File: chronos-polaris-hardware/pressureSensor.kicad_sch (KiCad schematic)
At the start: 3 parts, among them U9 BMP280

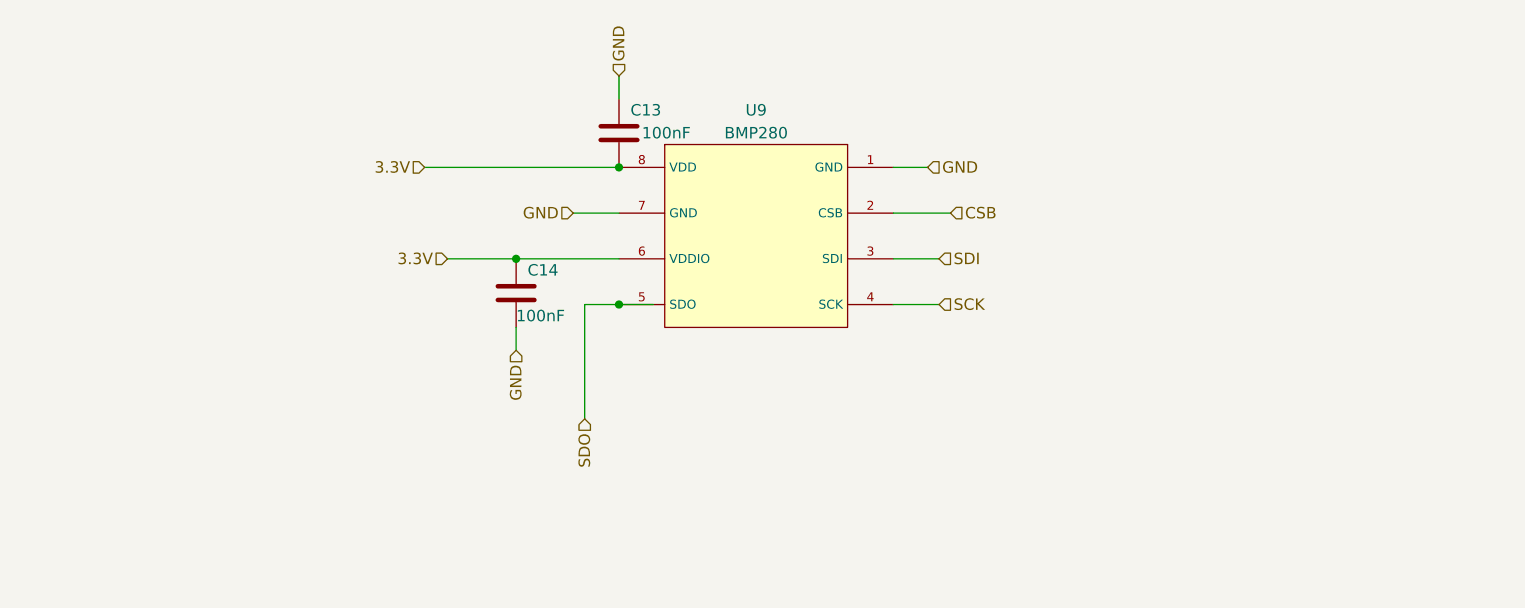
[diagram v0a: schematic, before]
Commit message: Schematic Changes as per DR1 Suggestions
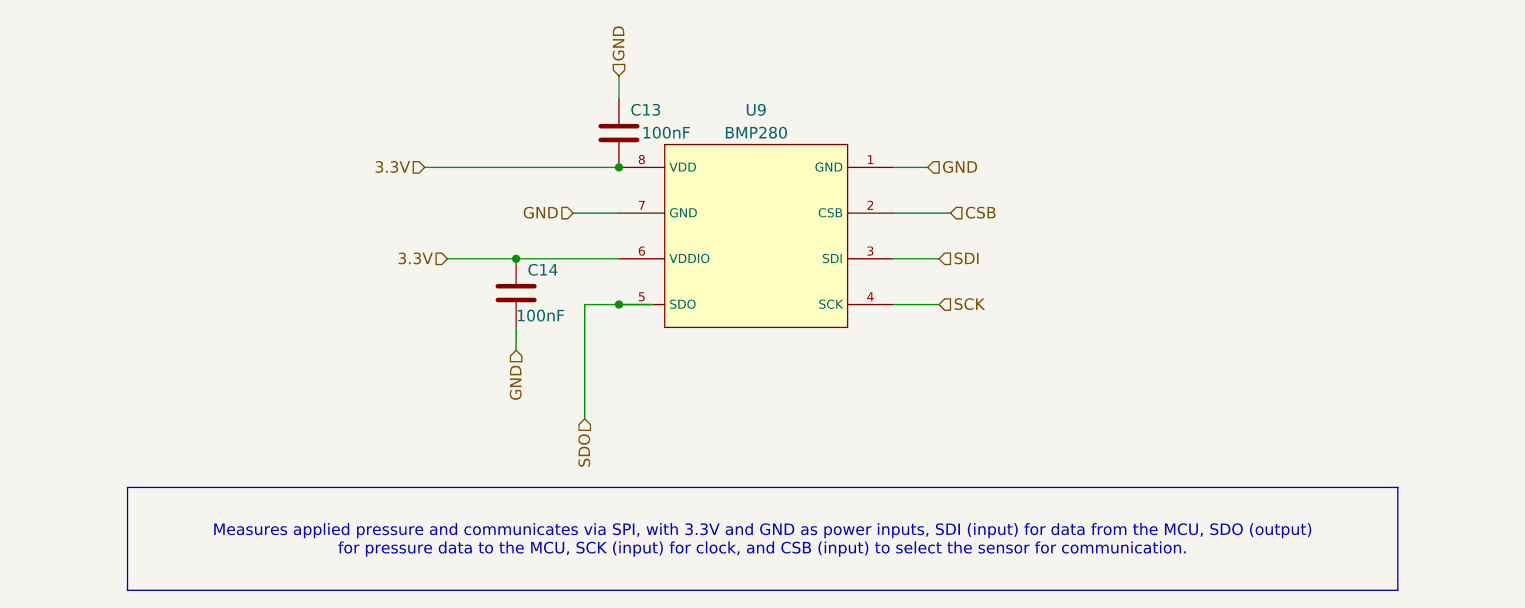
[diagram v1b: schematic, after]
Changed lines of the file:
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@@
+		)
+	)
+	(text_box " Measures applied pressure and communicates via SPI, with 3.3V and GND as power inputs, SDI (input) for data from the MCU, SDO (output) for pressure data to the MCU, SCK (input) for clock, and CSB (input) to select the sensor for communication."
+		(exclude_from_sim no)
+		(at 38.1 107.95 0)
+		(size 141.1463 11.43)
+		(stroke
+			(width 0)
+			(type default)
+		)
+		(fill
+			(type none)
+		)
+		(effects
+			(font
+				(size 1.27 1.27)
+			)
 		)
 	)

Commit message: fixes. - Rishik B.
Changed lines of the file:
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@@
 	)
 	(hierarchical_label "SDI"
-		(shape input)
+		(shape bidirectional)
 		(at 128.27 82.55 0)
 		(fields_autoplaced yes)
@@
 	)
 	(hierarchical_label "SDO"
-		(shape input)
+		(shape bidirectional)
 		(at 88.9 100.33 270)
 		(fields_autoplaced yes)
